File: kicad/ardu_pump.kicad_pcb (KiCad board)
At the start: 2 copper layers, 40 x 35 mm, 10 parts, among them J1 Conn_01x03_Male, J2 Conn_01x02_Female, J3 Conn_01x06_Male, Q1 Q_NPN_CBE, U1 ATtiny45-20PU, U2 HC-SR04

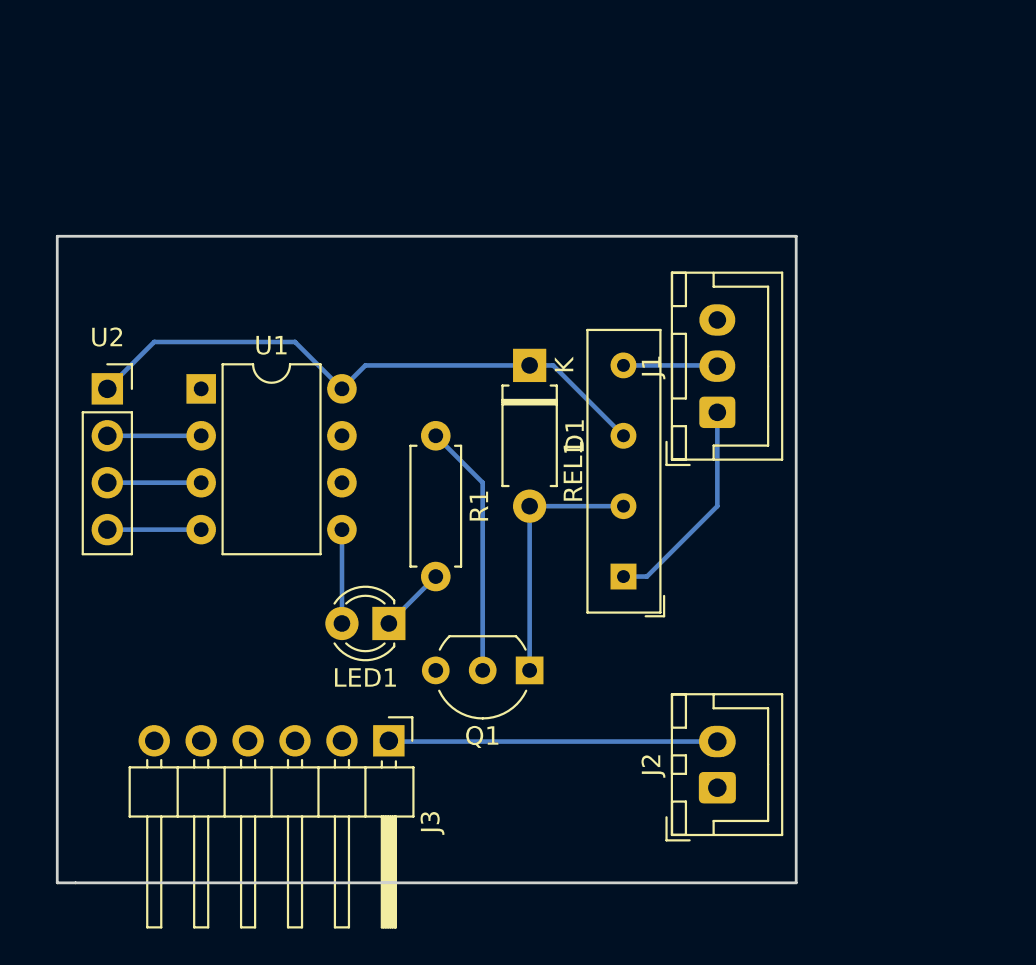
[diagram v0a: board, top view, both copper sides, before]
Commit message: Improving schematic.
Adding buttons and more powerful relay.
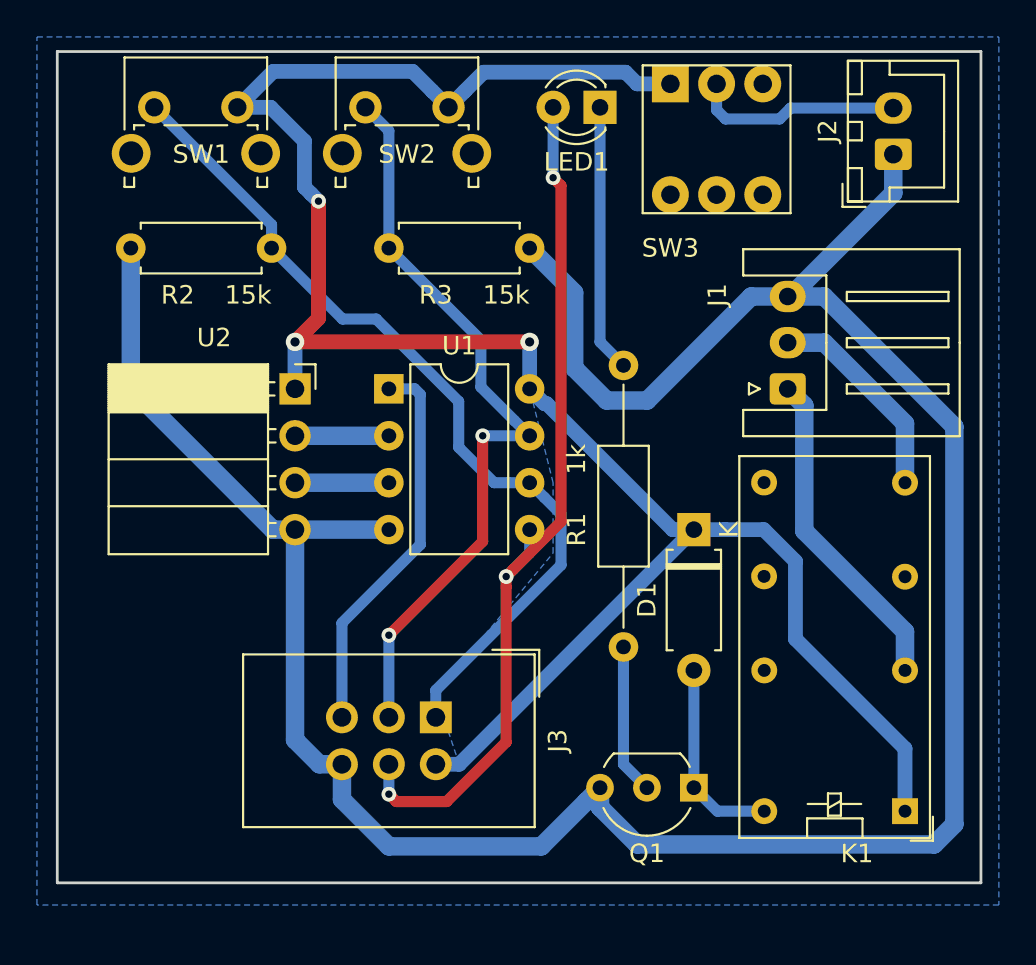
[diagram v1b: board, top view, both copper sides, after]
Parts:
- removed REL1: MSxx-1Axx-75, Relay_THT:Relay_SPST_StandexMeder_MS_Form1AB
- added G***: LOGO, N_logo:N_logo, F.Cu at (115.0, 52.4)
- added K1: G5V-2, Relay_THT:Relay_DPDT_Omron_G5V-2, F.Cu at (135.9, 71.1)
- added R2: 15k, Resistor_THT:R_Axial_DIN0207_L6.3mm_D2.5mm_P7.62mm_Horizontal, F.Cu at (94.0, 40.6)
- added R3: 15k, Resistor_THT:R_Axial_DIN0207_L6.3mm_D2.5mm_P7.62mm_Horizontal, F.Cu at (115.6, 40.6)
- added SW1: SW_Push, Button_Switch_THT:SW_Tactile_SPST_Angled_PTS645Vx58-2LFS, F.Cu at (95.2, 33.0)
- added SW2: SW_Push, Button_Switch_THT:SW_Tactile_SPST_Angled_PTS645Vx58-2LFS, F.Cu at (106.7, 33.0)
- added SW3: SW_DPDT_x2, switch-dpdt:SW_PUSH_8x8mm_DPDT, F.Cu at (123.2, 31.8)
- J1: footprint Connector_JST:JST_XH_B03B-XH-A_1x03_P2.50mm_Vertical -> Connector_JST:JST_XH_S03B-XH-A_1x03_P2.50mm_Horizontal
- J3: footprint Connector_PinHeader_2.54mm:PinHeader_1x06_P2.54mm_Horizontal -> Connector_IDC:IDC-Header_2x03_P2.54mm_Vertical
- R1: footprint Resistor_THT:R_Axial_DIN0207_L6.3mm_D2.5mm_P7.62mm_Horizontal -> Resistor_THT:R_Axial_DIN0207_L6.3mm_D2.5mm_P15.24mm_Horizontal
- U2: footprint Connector_PinSocket_2.54mm:PinSocket_1x04_P2.54mm_Vertical -> Connector_PinSocket_2.54mm:PinSocket_1x04_P2.54mm_Horizontal
- moved J2 35.6 mm to (135.3, 35.6)
- moved LED1 30.2 mm to (119.4, 33.0)
- moved R1 15.3 mm to (120.7, 62.2), turned to 90 degrees
- moved D1 12.6 mm to (124.5, 55.9)
- moved Q1 10.9 mm to (124.5, 69.8)
- moved U2 10.2 mm to (102.9, 48.3)
- moved U1 10.2 mm to (108.0, 48.3)
- moved J1 4.02 mm to (129.5, 48.3)
- moved J3 2.84 mm to (110.5, 66.0)
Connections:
- J2 pad 2: +5V -> Net-(J2-Pad2)
- J3 pad 1: +5V -> MISO
- J3 pad 2: GND -> +5V
- J3 pad 3: RST -> SCK
- J3 pad 4: SCK -> MOSI
- J3 pad 5: MOSI -> RST
- J3 pad 6: MISO -> GND
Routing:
- net GND: track 5.08 -> 144.7 mm
- net +5V: track 49.9 -> 113.4 mm, vias 0 -> 3
- net MISO: track 0.00 -> 47.1 mm
- net MOSI: track 5.08 -> 48.4 mm, vias 0 -> 3
- net SCK: track 0.00 -> 41.3 mm, vias 0 -> 2
- net RST: track 0.00 -> 21.1 mm
- net Net-(J2-Pad2): track 0.00 -> 11.4 mm
- net Net-(LED1-Pad1): track 3.59 -> 14.5 mm
- net Net-(J1-Pad2): track 5.10 -> 11.4 mm
- net Net-(J1-Pad1): track 11.7 -> 17.9 mm
- net Net-(Q1-Pad2): track 13.8 -> 8.15 mm
- net Net-(D1-Pad2): track 14.0 -> 10.7 mm
- added copper zone on B.Cu, net +5V
- added copper zone on B.Cu, net GND
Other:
- board size 40 x 35 mm -> 50 x 45 mm
- net class Default: clearance 0.2 -> 0.6; trace_width 0.25 -> 0.6
- net class Extra thick added: clearance 0.6, trace_width 1, via_dia 1, via_drill 0.5
- net class Normal added: clearance 0.6, trace_width 0.6, via_dia 0.8, via_drill 0.4
- net class Thick added: clearance 0.6, trace_width 0.8, via_dia 0.8, via_drill 0.4
- rule trace_clearance: 0.2 -> 0.6
